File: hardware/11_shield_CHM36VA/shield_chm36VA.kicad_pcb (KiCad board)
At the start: 2 copper layers, 199.6 x 100 mm, 71 parts, among them J10 Conn_01x06_Male, J11 Conn_01x10_Male, J12 Conn_01x10_Male, J14 Conn_01x09_Male, J15 Conn_01x02_Male, J17 Conn_01x06_Male, J20 Conn_01x09_Male, J21 Conn_01x02_Male, J23 Conn_01x10_Male, J25 Conn_01x02_Male, J26 Conn_01x10_Male, J27 Conn_01x10_Male, J28 Conn_02x05_Odd_Even, J29 Conn_02x05_Odd_Even, J3 Conn_01x06_Male, J30 Conn_02x20_Odd_Even, J31 Conn_02x20_Odd_Even, J32 Conn_02x10_Odd_Even, J33 Conn_02x20_Odd_Even, J4 Conn_01x04_Male, J5 Conn_01x10_Male, J7 Conn_01x04_Male, J8 Conn_02x05_Odd_Even, Q1 IRLL2705PBF, Q10 IRLL2705PBF, Q2 IRLL2705PBF, Q3 IRLL2705PBF, Q4 IRLL2705PBF, Q5 IRLL2705PBF, Q6 BSS138BKS, Q7 IRLL2705PBF, Q8 IRLL2705PBF, Q9 BSS138BKS, U1 LM217_TO-252, U2 AM26LS32ACD, U3 CNY17-1

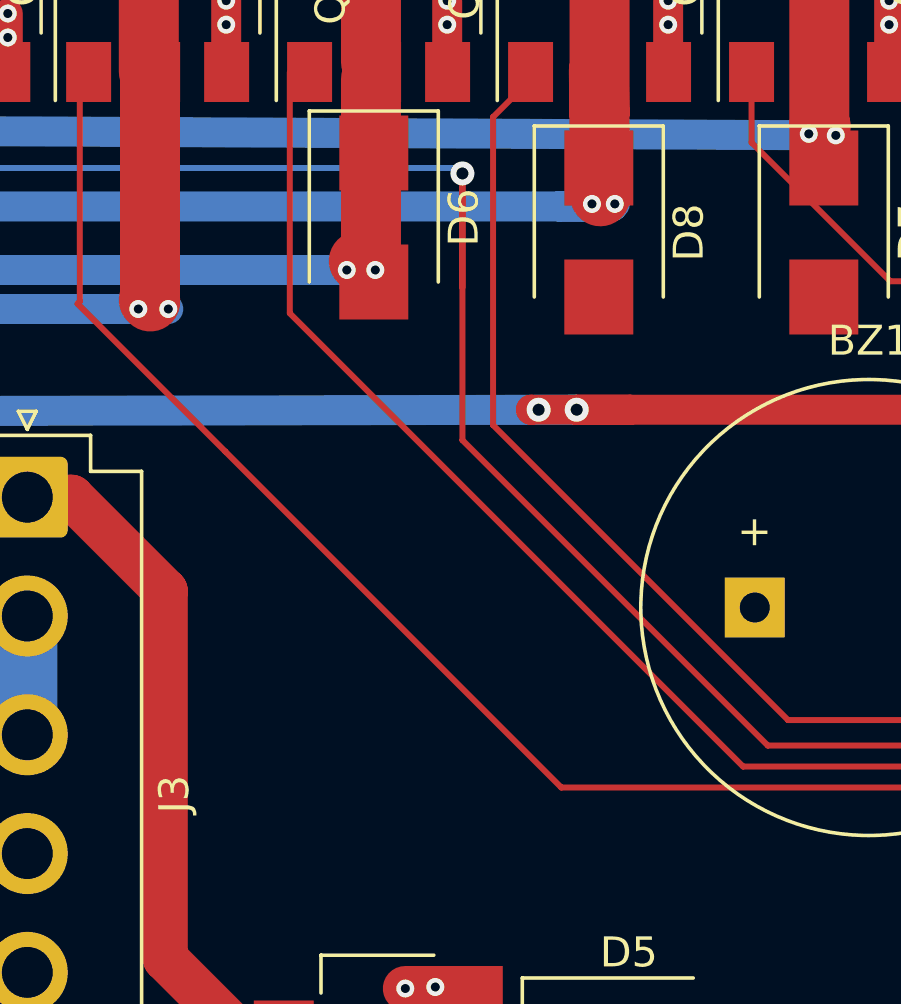
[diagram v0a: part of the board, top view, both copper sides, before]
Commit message: Schematics fixes - frewheeling diodes
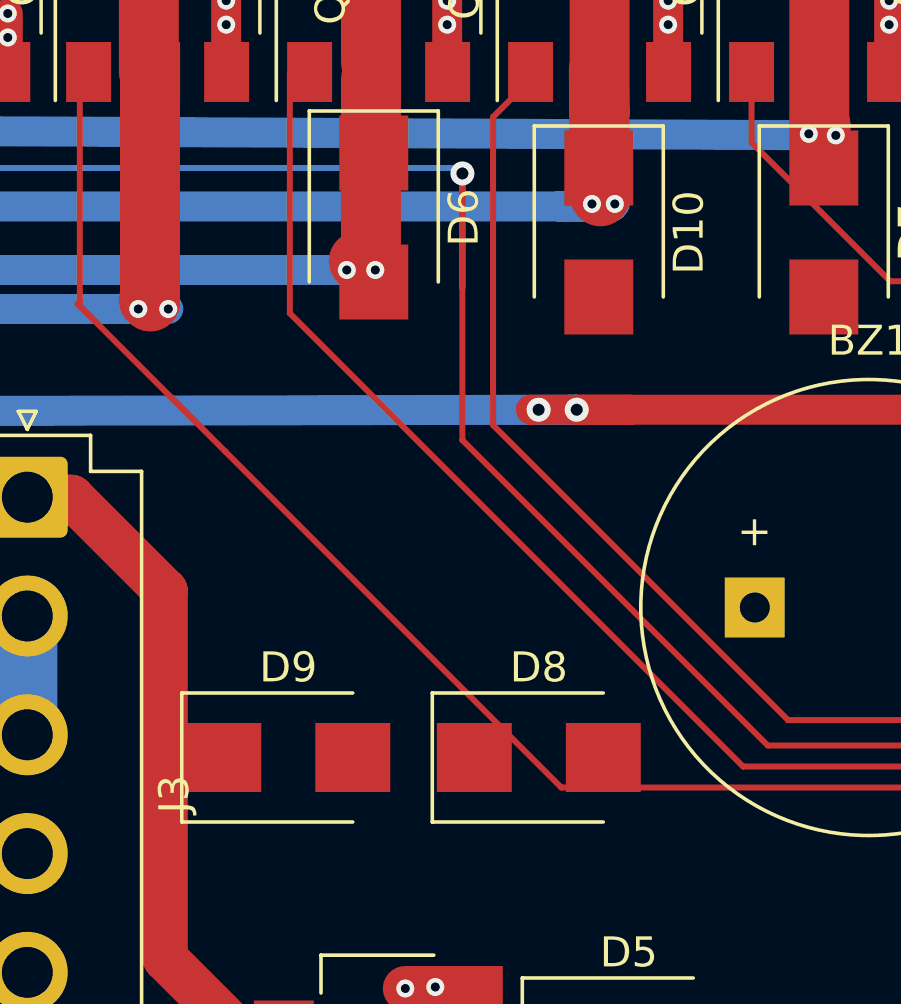
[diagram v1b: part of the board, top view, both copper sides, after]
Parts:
- added D8: SK56, Diode_SMD:D_SMB, F.Cu at (79.0, 85.0)
- added D9: SK56, Diode_SMD:D_SMB, F.Cu at (70.7, 85.0)
- renumbered D8 to D10
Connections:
- D10 pad 1: /controller/OUT_N2_VALVE -> +24V
- D10 pad 2: GND -> /controller/OUT_N2_VALVE
- D3 pad 1: /controller/OUT_LZ -> +24V
- D3 pad 2: GND -> /controller/OUT_LZ
- D4 pad 1: /controller/PUMP_VACUUM -> +24V
- D4 pad 2: GND -> /controller/PUMP_VACUUM
- D5 pad 1: /controller/PUMP_PRESS -> +24V
- D5 pad 2: GND -> /controller/PUMP_PRESS
- D6 pad 1: /controller/OUT_N1_VALVE -> +24V
- D6 pad 2: GND -> /controller/OUT_N1_VALVE
- D7 pad 1: /controller/OUT_UNUSED -> +24V
- D7 pad 2: GND -> /controller/OUT_UNUSED
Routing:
- net /controller/ENC_X_A-: track 112.6 -> 0.00 mm, vias 2 -> 0
- net /controller/ENC_X_A+: track 0.00 -> 112.6 mm, vias 0 -> 2
- net /controller/DIR_C: track 98.3 -> 0.00 mm, vias 1 -> 0
- net /controller/STEP_C: track 103.9 -> 202.2 mm, vias 1 -> 2
